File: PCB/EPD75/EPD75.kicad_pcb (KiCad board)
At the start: 2 copper layers, 168 x 110 mm, 129 parts, among them J1 Conn_01x26, J10 TF_PUSH, J11 Reset, J12 TC2030-USB-NL-DS, J4 BTN1, J5 USB-C-Socket-V, J6 BTN2, J7 USB-C-Socket-V, J8 PWR, J9 PWR, P1 2, P10 D+, P11 D-, P12 5V, P13 O, P14 O, P15 +, P16 -, P17 +, P18 -, P2 1, P3 -, P4 -, P5 2, P6 1, P7 +, P8 +, P9 GND, Q1 BSS138, U1 G3VM-41GR8, U3 MD8942, U4 ESP32-S3-MINI-1

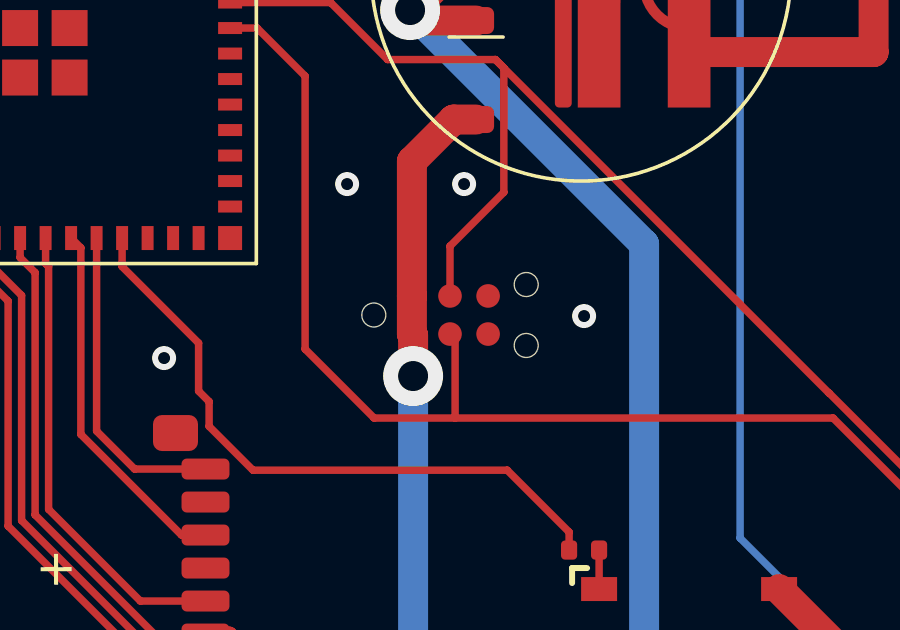
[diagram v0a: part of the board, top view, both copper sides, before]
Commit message: Update for new USB leads
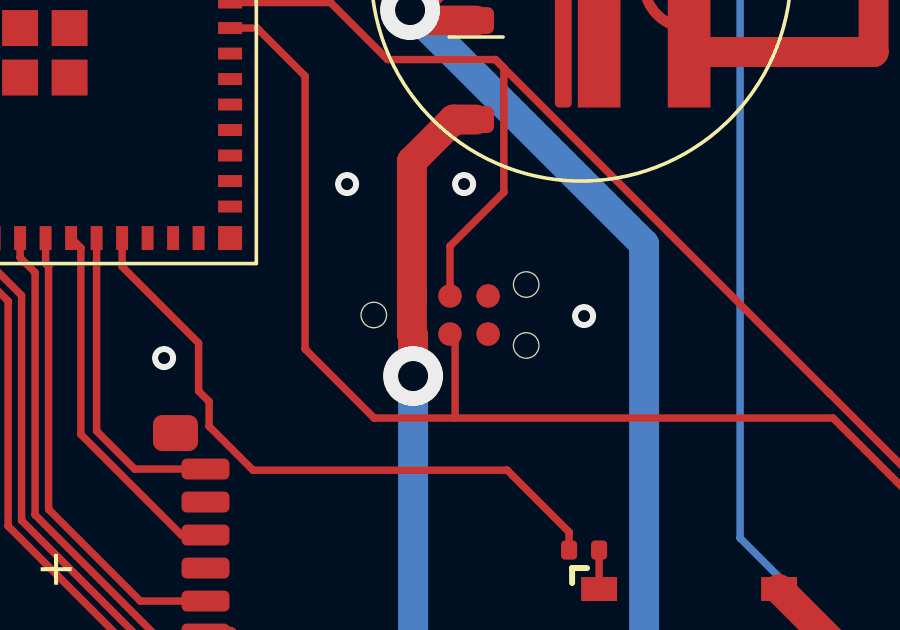
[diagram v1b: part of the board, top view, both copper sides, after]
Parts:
- added REF**: Shadow, RevK:Shadow, F.Cu at (100.0, 100.0)

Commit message: New connectors
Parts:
- removed J9: PWR, RevK:PTSM-HH-2-RA-SMD
- removed P15: +, RevK:SolderPad
- removed P16: -, RevK:SolderPad
- added J2: PWR, RevK:WAGO-2060-452-998-404, F.Cu at (48.5, 132.5)
- added J3: RELAY, RevK:WAGO-2060-452-998-404, F.Cu at (58.0, 132.6)
- J4, J6, J8: footprint RevK:PTSM-HH-2-RA-SMD -> RevK:WAGO-2060-452-998-404
- moved J8 106.2 mm to (151.8, 119.0), turned to 180 degrees
- moved C28 4.74 mm to (135.0, 116.5), turned to 0 degrees
- moved D34 1.11 mm to (144.0, 131.0)
- moved J4 1.00 mm to (152.0, 131.0), turned to 180 degrees
- moved D13 0.18 mm to (144.0, 69.0)
- turned J6 to 180 degrees
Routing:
- net Net-(J3-Pin_1): track 35.6 -> 54.0 mm
- net Net-(J3-Pin_2): track 43.3 -> 51.1 mm
- net VBUS: track 190.6 -> 184.8 mm
- net Net-(J4-Pin_2): track 183.3 -> 188.2 mm
- net PWR: track 373.3 -> 368.9 mm
- net Net-(J6-Pin_2): track 164.6 -> 168.3 mm
- net RELAY: track 21.5 -> 22.1 mm

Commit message: No hole
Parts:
- moved C28 4.30 mm to (138.5, 119.0)
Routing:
- net VBUS: track 184.8 -> 189.3 mm
- net +3.3V: track 853.5 -> 849.5 mm
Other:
- outline, holes or cut-outs redrawn

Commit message: Major tidy
Signed-off-by: RevK <github@e.gg>
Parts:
- removed D13, D20, D4, D7: ~, RevK:DFN1006-2L
- removed J2: PWR, RevK:WAGO-2060-452-998-404
- removed P1, P5: 2, RevK:SolderPad
- removed P10: D+, RevK:SolderPad
- removed P11: D-, RevK:SolderPad
- removed P12: 5V, RevK:SolderPad
- removed P13, P14: O, RevK:SolderPad
- removed P17, P7, P8: +, RevK:SolderPad
- removed P18, P3, P4: -, RevK:SolderPad
- removed P2, P6: 1, RevK:SolderPad
- removed P9: GND, RevK:SolderPad
- moved J3 95.0 mm to (152.0, 119.0), turned to 180 degrees
- moved R14 88.7 mm to (136.5, 116.0)
- moved U1 88.7 mm to (140.0, 119.0)
- moved J12 64.5 mm to (104.7, 129.4), turned to 180 degrees
- moved J8 38.0 mm to (152.0, 81.0)
- moved C28 35.6 mm to (109.0, 139.0)
- moved J11 30.2 mm to (29.0, 62.0), turned to 90 degrees
- moved D6 29.0 mm to (27.0, 78.0)
- moved R10 28.5 mm to (33.9, 72.1)
- moved C10 28.5 mm to (32.0, 76.0)
- moved C19 28.5 mm to (27.0, 73.0)
- moved C8 28.5 mm to (29.5, 75.3)
- moved C9 28.5 mm to (34.5, 75.3)
- moved L2 28.5 mm to (32.0, 78.6)
- moved R11 28.5 mm to (30.2, 72.1)
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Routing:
- net PWR: track 368.9 -> 165.0 mm, vias 4 -> 2
- net RELAY: track 22.1 -> 108.1 mm, vias 0 -> 2
- net +3.3V: track 849.5 -> 902.8 mm
- net VBUS: track 189.3 -> 231.7 mm
- net Net-(J3-Pin_1): track 54.0 -> 14.0 mm
- net Net-(J3-Pin_2): track 51.1 -> 14.0 mm
- net Net-(J4-Pin_2): track 188.2 -> 154.7 mm
- net Net-(J11-Pin_2): track 17.1 -> 43.7 mm, vias 0 -> 2
- net Net-(J6-Pin_2): track 168.3 -> 173.4 mm
- net D-: track 169.0 -> 173.4 mm, vias 0 -> 2
- net D+: track 173.3 -> 171.1 mm
- net GND: track 19.9 -> 21.2 mm
- net BTN2: track 5.95 -> 5.26 mm
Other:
- outline, holes or cut-outs redrawn
- board text added: "${CURRENT_DATE}"
- board text added: "3 4 5 6 7"
- board text added: "40 39 38 37 36 35"
- board text added: "41"
- board text added: "42"
- board text added: "8"
- board text added: "B"
- board text added: "MOSI CLK CS DC RST BUSY"
- board text added: "Made in China for Andrews & Arnold Ltd"
- board text added: "SDSS SDMOSI SDSCK SDMISO SDCD"
- board text added: "Thanks to xkcd.com for images on this PCB"
- board text removed: "42 41 40 39 38 37 36 35 2 3 4 5 6 7 8"
- board text removed: "BA"
- board text removed: "BTN2 BTN1 MOSI CLK CS DC RST BUSY RGB*24 SDSS SDMOSI SDSCK SDMISO SDCD RELAY"
- board text removed: "Made in China for Andrews & Arnold Ltd ${CURRENT_DATE}"
- board text removed: "O"
- board text removed: "Thanks to xkcd.com"
